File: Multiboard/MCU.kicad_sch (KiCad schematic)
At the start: 48 parts, among them J1 Conn_01x20_Socket, J2 Conn_01x20_Socket, J3 Debug, J4 USB_C_Receptacle_USB2.0_16P, SW1 BOOT0, SW2 NRST, SW8 KEY, U1 STM32F411RET6, U2 MAX662AESA_T, U3 MCP1792x-3302xCB, Y1 32.768KHz, Y2 25MHz

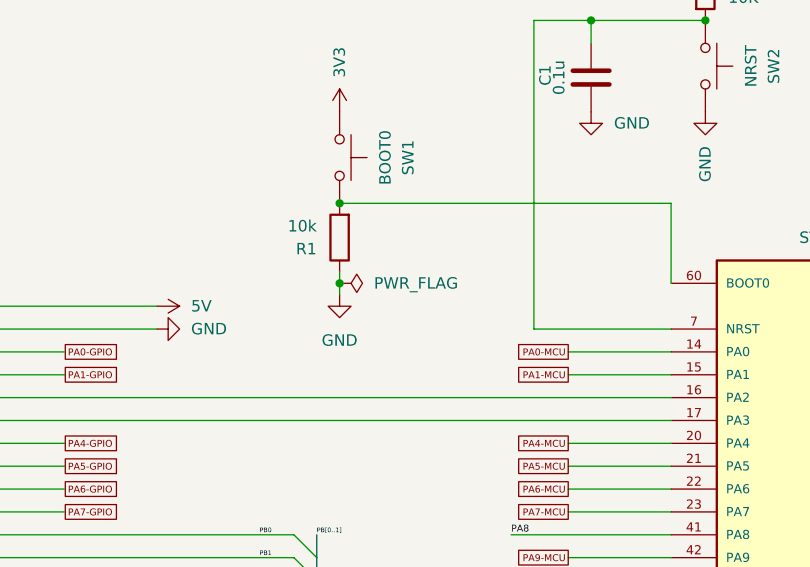
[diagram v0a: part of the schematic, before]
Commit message: added and wired banks to the fpga schematic
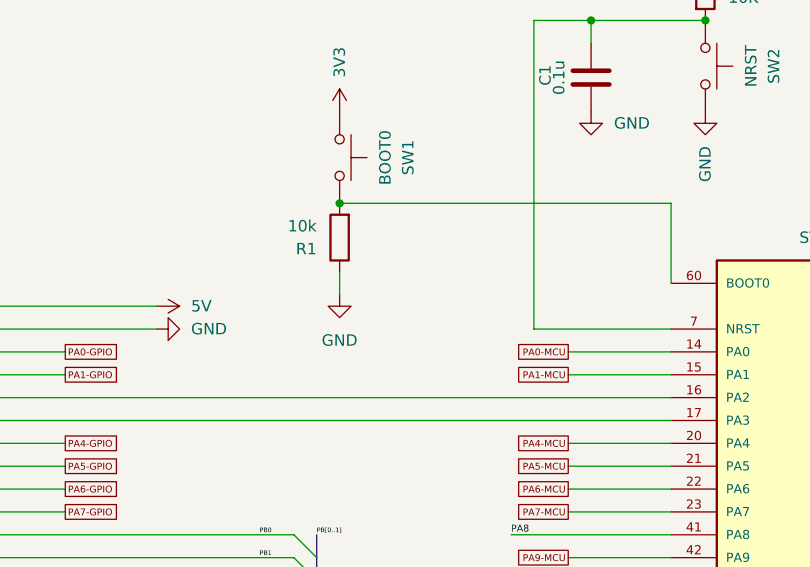
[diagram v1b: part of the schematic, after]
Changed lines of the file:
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@@
 	)
 	(junction
-		(at 119.38 59.69)
-		(diameter 0)
-		(color 0 0 0 0)
-	)
-	(junction
 		(at 119.38 50.8)
 		(diameter 0)
@@
 	(wire
 		(pts
-			(xy 119.38 59.69) (xy 119.38 58.42)
+			(xy 119.38 58.42) (xy 119.38 60.96)
 		)
 		(stroke
@@
 	(wire
 		(pts
-			(xy 119.38 60.96) (xy 119.38 59.69)
-		)
-		(stroke
-			(width 0)
-			(type default)
-		)
-	)
-	(wire
-		(pts
 			(xy 146.05 146.05) (xy 146.05 153.67)
 		)
@@
 					(unit 1)
 				)
-			)
-		)
-	)
-	(symbol
-		(lib_id "power:PWR_FLAG")
-		(at 119.38 59.69 270)
-		(unit 1)
-		(exclude_from_sim no)
-		(in_bom yes)
-		(on_board yes)
-		(dnp no)
-		(fields_autoplaced yes)
-		(property "Reference" "#FLG03"
-			(at 121.285 59.69 0)
-			(effects
-				(font
-					(size 1.27 1.27)
-				)
-				(hide yes)
-			)
-		)
-		(property "Value" "PWR_FLAG"
-			(at 123.19 59.6899 90)
-			(effects
-				(font
-					(size 1.27 1.27)
-				)
-				(justify left)
-			)
-		)
-		(property "Footprint" ""
-			(at 119.38 59.69 0)
-			(effects
-				(font
-					(size 1.27 1.27)
-				)
-				(hide yes)
-			)
-		)
-		(property "Datasheet" "~"
-			(at 119.38 59.69 0)
-			(effects
-				(font
-					(size 1.27 1.27)
-				)
-				(hide yes)
-			)
-		)
-		(property "Description" "Special symbol for telling ERC where power comes from"
-			(at 119.38 59.69 0)
-			(effects
-				(font
-					(size 1.27 1.27)
-				)
-				(hide yes)
-			)
-		)
-		(pin "1"
-		)
-		(instances
-			(project "Multiboard"
-				(path "/9ed4a389-3aa7-41f1-b239-280eb7f09ef1/2bca3eb5-73b3-4aa8-9f30-e1743a374253"
-					(reference "#FLG03")
-					(unit 1)
-				)

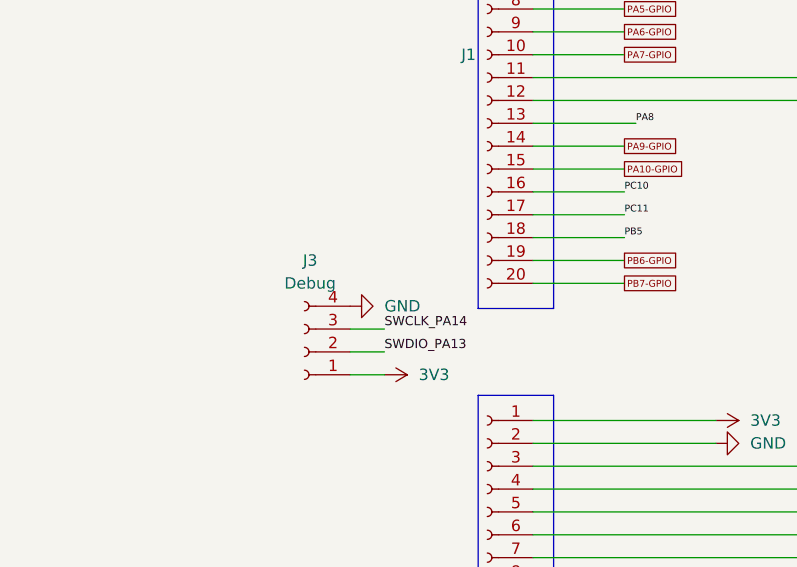
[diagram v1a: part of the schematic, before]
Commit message: Added footprints and fixed schematic
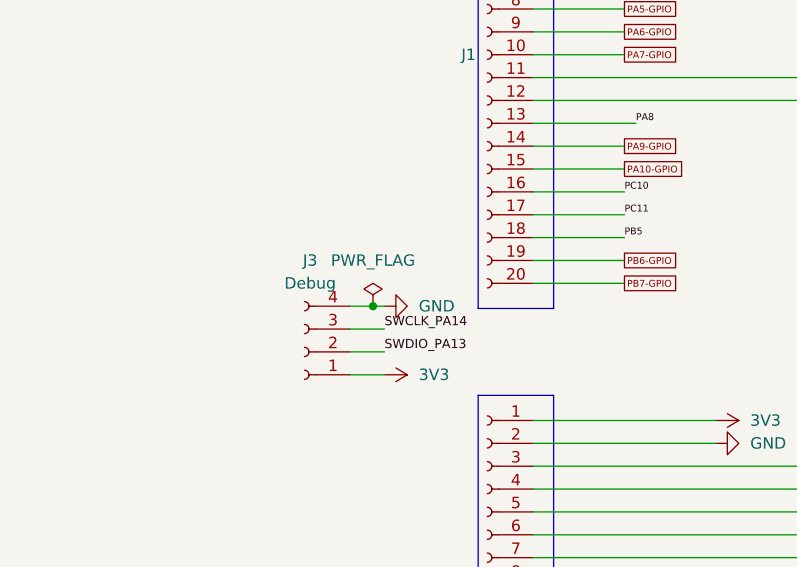
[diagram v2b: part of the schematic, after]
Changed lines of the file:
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@@
 	)
 	(junction
+		(at 60.96 113.03)
+		(diameter 0)
+		(color 0 0 0 0)
+	)
+	(junction
 		(at 238.76 60.96)
 		(diameter 0)
@@
 	(wire
 		(pts
+			(xy 62.23 113.03) (xy 60.96 113.03)
+		)
+		(stroke
+			(width 0)
+			(type default)
+		)
+	)
+	(wire
+		(pts
 			(xy 208.28 64.77) (xy 208.28 63.5)
 		)
@@
 	(wire
 		(pts
+			(xy 58.42 113.03) (xy 60.96 113.03)
+		)
+		(stroke
+			(width 0)
+			(type default)
+		)
+	)
+	(wire
+		(pts
 			(xy 356.87 123.19) (xy 364.49 123.19)
 		)
@@
 	)
 	(symbol
+		(lib_id "power:PWR_FLAG")
+		(at 60.96 113.03 0)
+		(unit 1)
+		(exclude_from_sim no)
+		(in_bom yes)
+		(on_board yes)
+		(dnp no)
+		(fields_autoplaced yes)
+		(property "Reference" "#FLG010"
+			(at 60.96 111.125 0)
+			(effects
+				(font
+					(size 1.27 1.27)
+				)
+				(hide yes)
+			)
+		)
+		(property "Value" "PWR_FLAG"
+			(at 60.96 107.95 0)
+			(effects
+				(font
+					(size 1.27 1.27)
+				)
+			)
+		)
+		(property "Footprint" ""
+			(at 60.96 113.03 0)
+			(effects
+				(font
+					(size 1.27 1.27)
+				)
+				(hide yes)
+			)
+		)
+		(property "Datasheet" "~"
+			(at 60.96 113.03 0)
+			(effects
+				(font
+					(size 1.27 1.27)
+				)
+				(hide yes)
+			)
+		)
+		(property "Description" "Special symbol for telling ERC where power comes from"
+			(at 60.96 113.03 0)
+			(effects
+				(font
+					(size 1.27 1.27)
+				)
+				(hide yes)
+			)
+		)
+		(pin "1"
+		)
+		(instances
+			(project "Multiboard"
+				(path "/9ed4a389-3aa7-41f1-b239-280eb7f09ef1/2bca3eb5-73b3-4aa8-9f30-e1743a374253"
+					(reference "#FLG010")
+					(unit 1)
+				)
+			)
+		)
+	)
+	(symbol
 		(lib_id "Device:L_Iron")
 		(at 223.52 69.85 90)
@@
 	(symbol
 		(lib_id "power:GND")
-		(at 58.42 113.03 90)
+		(at 62.23 113.03 90)
 		(unit 1)
 		(exclude_from_sim no)
@@
 		(fields_autoplaced yes)
 		(property "Reference" "#PWR020"
-			(at 64.77 113.03 0)
+			(at 68.58 113.03 0)
 			(effects
 				(font
@@
 		)
 		(property "Value" "GND"
-			(at 62.23 113.0299 90)
+			(at 66.04 113.0299 90)
 			(effects
 				(font
@@
 		)
 		(property "Footprint" ""
-			(at 58.42 113.03 0)
+			(at 62.23 113.03 0)
 			(effects
 				(font
@@
 		)
 		(property "Datasheet" ""
-			(at 58.42 113.03 0)
+			(at 62.23 113.03 0)
 			(effects
 				(font
@@
 		)
 		(property "Description" "Power symbol creates a global label with name \"GND\" , ground"
-			(at 58.42 113.03 0)
+			(at 62.23 113.03 0)
 			(effects
 				(font

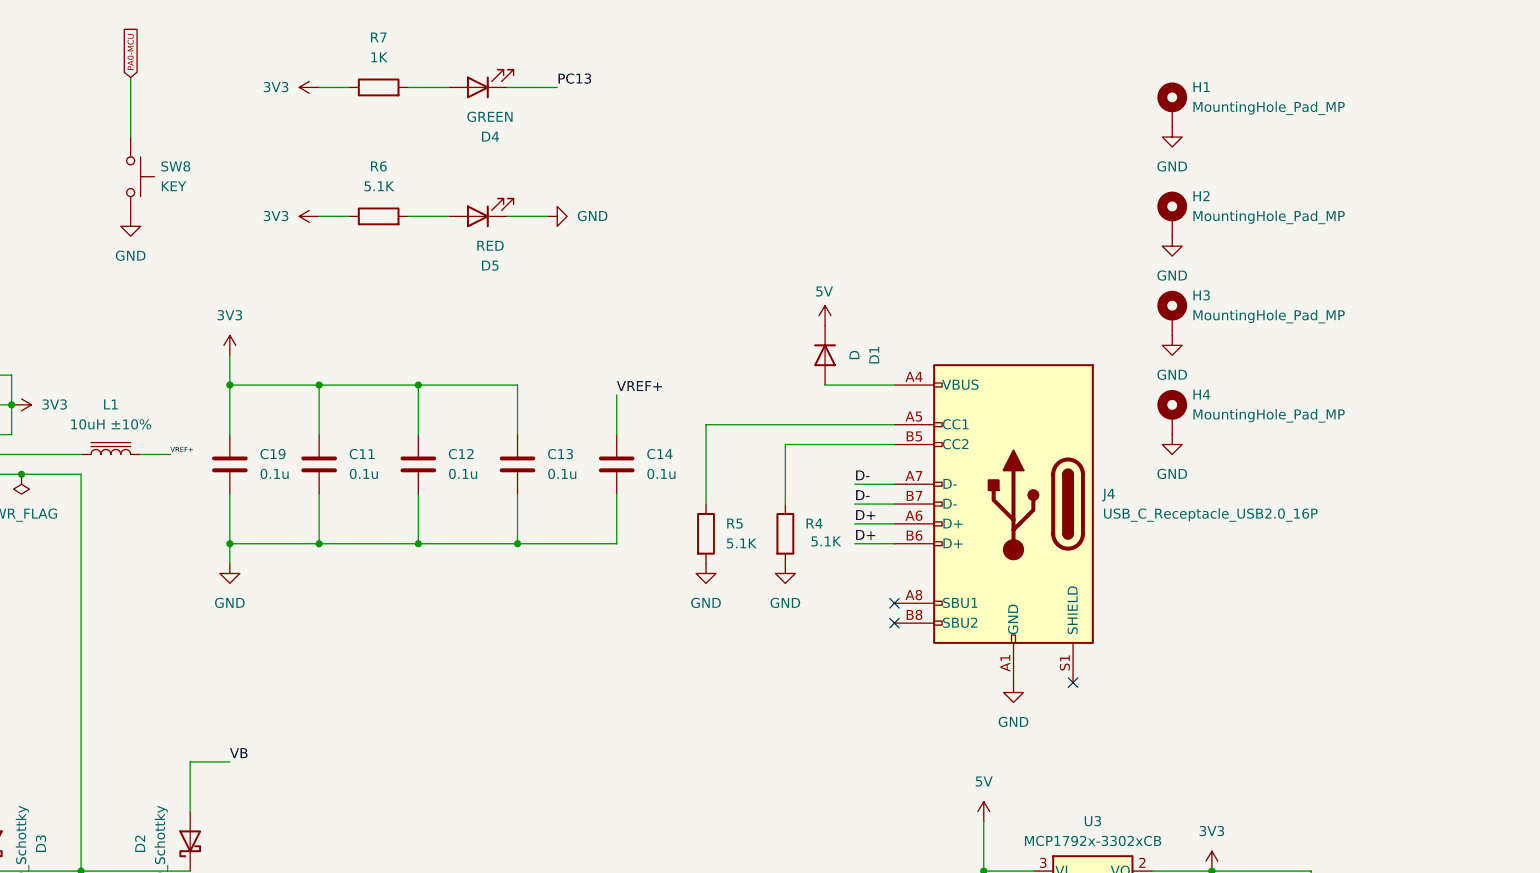
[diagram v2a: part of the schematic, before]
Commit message: Completed mcu usb-c, mcu oscillators and mcu jtag pins
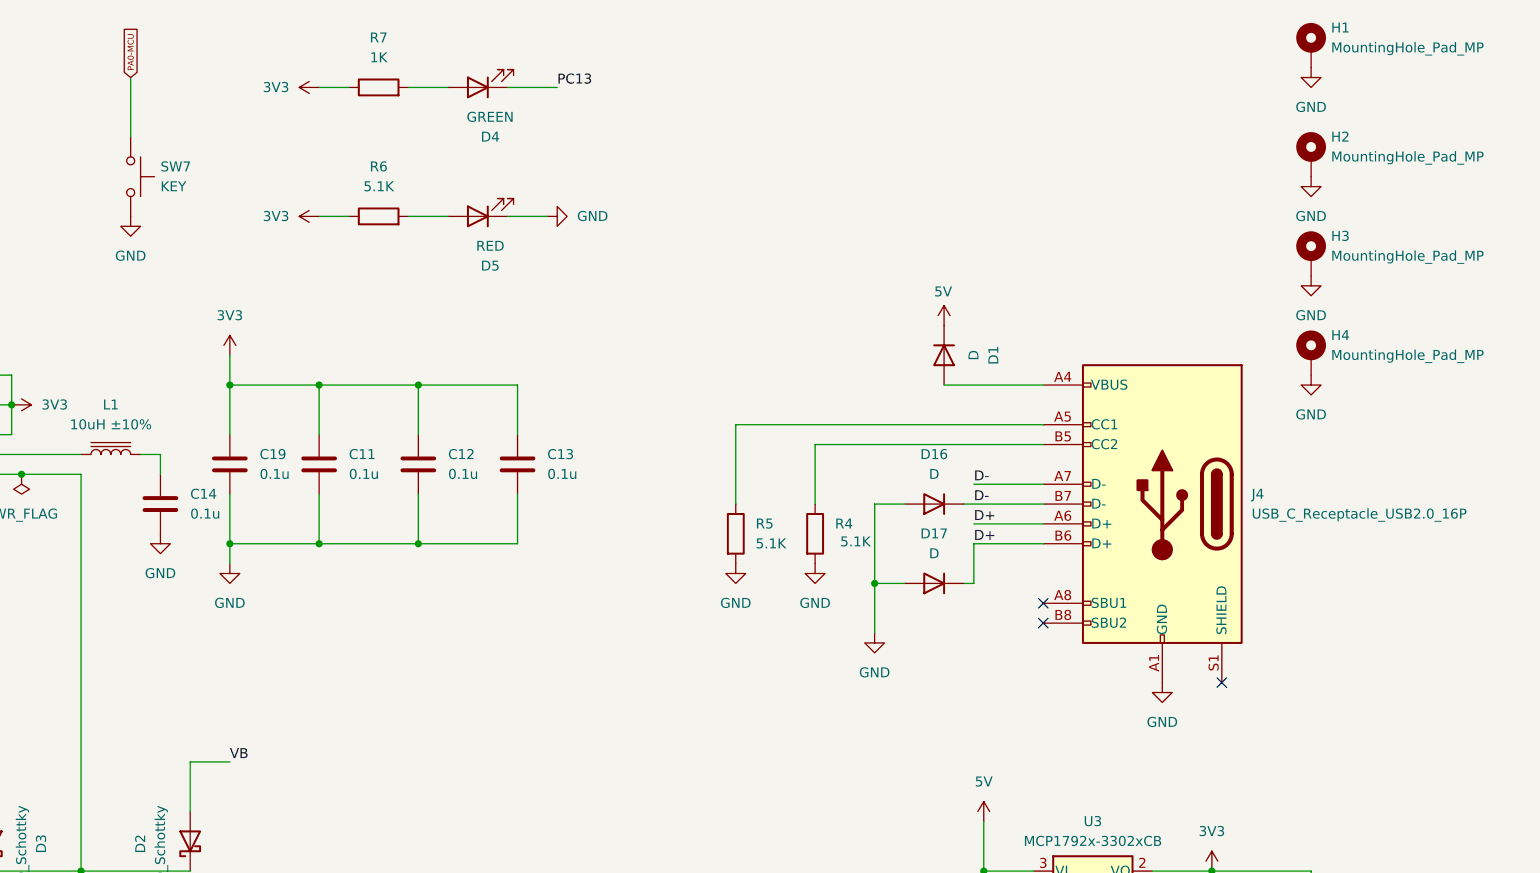
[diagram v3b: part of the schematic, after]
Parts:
- added D16, D17: D, Diode_SMD:D_0603_1608Metric_Pad1.05x0.95mm_HandSolder, symbol Device:D
- Y2: footprint Crystal:Crystal_SMD_HC49-SD -> Crystal:Crystal_SMD_3225-4Pin_3.2x2.5mm
- renumbered SW8 to SW7
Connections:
- net D+: now also D17.1 (K)
- net D-: now also D16.1 (K)
- net GND: now also C14.1, D16.2 (A), D17.2 (A); no longer C14.2
- net at C4.2, U1.5 (PH0-OSC_IN): now also Y2.3; no longer Y2.2
- net VREF+: no longer names the net of L1.2
- net VREF+: now also C14.2; no longer C14.1
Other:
- moved on the sheet: C14, D1, H1, H2, H3, H4, J4, R4, R5
